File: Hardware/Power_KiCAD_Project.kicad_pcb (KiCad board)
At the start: 4 copper layers, 80 x 93.2 mm, 83 parts, among them J1 Barrel_Jack_MountingPin, J2 XT60 Cell 5, J3 XT60 Cell 4, J4 XT60 Cell 3, J5 XT60 Cell 2, J6 XT60 Cell 1, J7 XT60 To External Switch, J8 L717SDC37P1ACH4F, Q1 PSMN2R6-40YS, Q2 BSS84PH6327XTSA2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

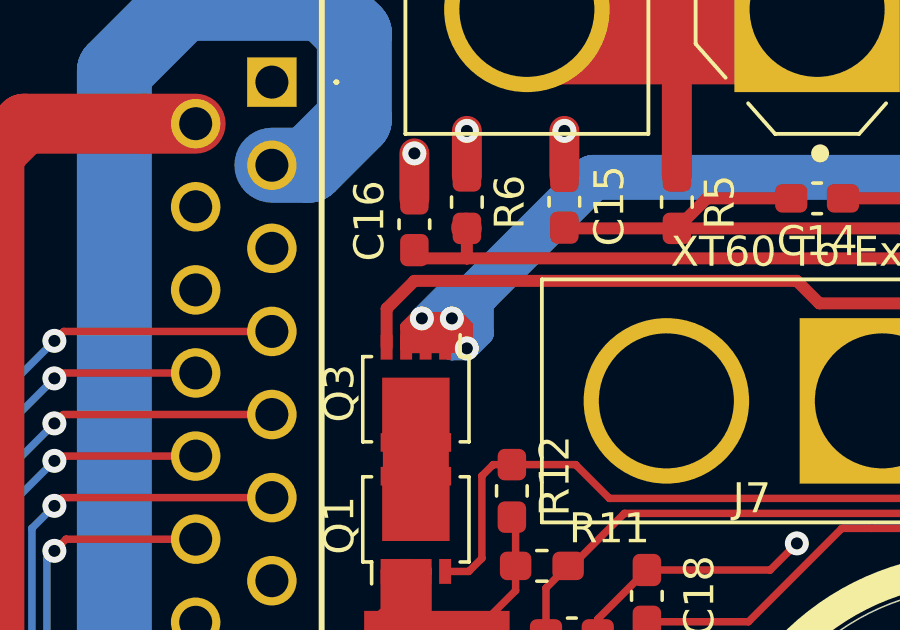
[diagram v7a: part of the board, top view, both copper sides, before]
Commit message: Adjustments to inner copper pours
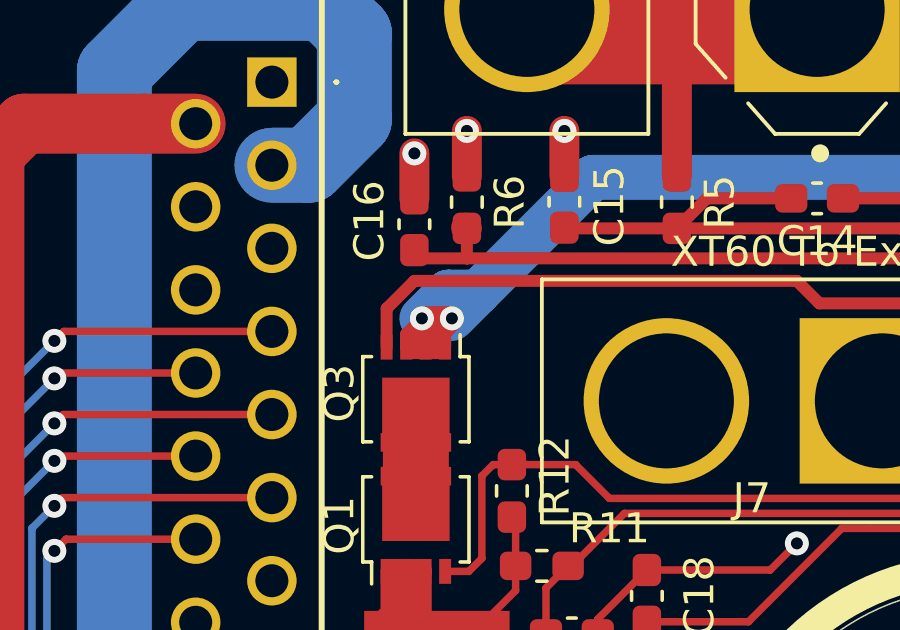
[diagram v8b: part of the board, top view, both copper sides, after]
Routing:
- net /LiPo Pack Monitor/PACK-: track 95.9 -> 82.5 mm, vias 4 -> 3
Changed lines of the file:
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@@
     (thickness 1.6)
     (drawings 27)
-    (tracks 936)
+    (tracks 909)
     (zones 0)
     (modules 83)
@@
     (user_trace_width 5)
     (trace_clearance 0.05)
-    (zone_clearance 1)
+    (zone_clearance 0.508)
     (zone_45_only no)
     (trace_min 0.09)
@@
   (segment (start 134 126.4) (end 135.25 126.4) (width 0.25) (layer B.Cu) (net 80))
   (segment (start 133.4 125.8) (end 134 126.4) (width 0.25) (layer B.Cu) (net 80))
-  (segment (start 98.774999 82.46) (end 98.124999 82.46) (width 0.4) (layer F.Cu) (net 147))
-  (segment (start 97.475 82.460001) (end 98.124999 82.46) (width 0.4) (layer F.Cu) (net 147))
-  (segment (start 98.775 82.46) (end 99.21 82.46) (width 0.4) (layer F.Cu) (net 147))
-  (segment (start 98.125 82.46) (end 98.29 82.46) (width 0.4) (layer F.Cu) (net 147))
-  (segment (start 97.475 82.46) (end 97.475 82.275) (width 0.4) (layer F.Cu) (net 147))
-  (segment (start 98.315 82) (end 98.775 82.46) (width 0.4) (layer F.Cu) (net 147))
-  (segment (start 97.475 82.275) (end 97.75 82) (width 0.4) (layer F.Cu) (net 147))
-  (segment (start 97.75 82) (end 98.315 82) (width 0.4) (layer F.Cu) (net 147))
-  (segment (start 97.75 82) (end 98.25 81.5) (width 0.4) (layer F.Cu) (net 147))
-  (segment (start 97.75 82.085) (end 98.125 82.46) (width 0.4) (layer F.Cu) (net 147))
-  (segment (start 97.75 82) (end 97.75 82.085) (width 0.4) (layer F.Cu) (net 147))
-  (segment (start 98.25 81.5) (end 99 81.5) (width 0.4) (layer F.Cu) (net 147))
-  (segment (start 98.25 81.5) (end 98.75 82) (width 0.4) (layer F.Cu) (net 147))
-  (segment (start 98.29 82.46) (end 98.75 82) (width 0.4) (layer F.Cu) (net 147))
-  (segment (start 98.75 81.5) (end 99 81.75) (width 0.4) (layer F.Cu) (net 147))
-  (segment (start 98.25 81.5) (end 98.75 81.5) (width 0.4) (layer F.Cu) (net 147))
-  (segment (start 99 81.75) (end 99.25 81.5) (width 0.4) (layer F.Cu) (net 147))
-  (segment (start 98.75 82) (end 99 81.75) (width 0.4) (layer F.Cu) (net 147))
-  (segment (start 99.5 81.75) (end 99.25 81.5) (width 0.4) (layer F.Cu) (net 147))
-  (segment (start 98.75 81.5) (end 99.5 82.25) (width 0.4) (layer F.Cu) (net 147))
-  (segment (start 98.25 81.5) (end 97.75 81.5) (width 0.4) (layer F.Cu) (net 147))
-  (segment (start 97.475 81.775) (end 97.475 82.46) (width 0.4) (layer F.Cu) (net 147))
-  (segment (start 97.75 81.5) (end 97.475 81.775) (width 0.4) (layer F.Cu) (net 147))
-  (segment (start 99.5 82.5) (end 99.5 81.75) (width 0.4) (layer F.Cu) (net 147))
-  (via (at 99.5 82.5) (size 0.8) (drill 0.4) (layers F.Cu B.Cu) (net 147))
   (via (at 120.5 83.25) (size 0.8) (drill 0.4) (layers F.Cu B.Cu) (net 147))
   (segment (start 120.375 83.125) (end 120.5 83.25) (width 0.4) (layer F.Cu) (net 147))
   (segment (start 119.25 83.125) (end 120.375 83.125) (width 0.4) (layer F.Cu) (net 147))
-  (segment (start 99 81.5) (end 99.25 81.5) (width 0.4) (layer F.Cu) (net 147))
   (via (at 99 81.5) (size 0.8) (drill 0.4) (layers F.Cu B.Cu) (net 147))
-  (segment (start 97.75 81.5) (end 97.75 81.5) (width 0.4) (layer F.Cu) (net 147))
   (via (at 98 81.5) (size 0.8) (drill 0.4) (layers F.Cu B.Cu) (net 147))
   (segment (start 154.5 71.25) (end 151 67.75) (width 1.5) (layer B.Cu) (net 147))
   (segment (start 154.5 75.25) (end 154.5 71.25) (width 1.5) (layer B.Cu) (net 147))
   (segment (start 152.950001 76.799999) (end 154.5 75.25) (width 1.5) (layer B.Cu) (net 147))
-  (segment (start 98.875 80.625) (end 99.875 80.625) (width 0.8) (layer B.Cu) (net 147))
-  (segment (start 98 81.5) (end 98.875 80.625) (width 0.8) (layer B.Cu) (net 147))
   (segment (start 99.875 80.625) (end 103.700001 76.799999) (width 1.5) (layer B.Cu) (net 147))
-  (segment (start 99 81.5) (end 99.875 80.625) (width 1.5) (layer B.Cu) (net 147))
-  (segment (start 99.5 82) (end 99 81.5) (width 0.8) (layer B.Cu) (net 147))
-  (segment (start 99.5 82.5) (end 99.5 82) (width 0.8) (layer B.Cu) (net 147))
-  (segment (start 99 82.5) (end 98 81.5) (width 0.8) (layer B.Cu) (net 147))
-  (segment (start 99.5 82.5) (end 99 82.5) (width 0.8) (layer B.Cu) (net 147))
-  (segment (start 99.5 82.5) (end 100 82) (width 0.8) (layer B.Cu) (net 147))
   (segment (start 100 80.75) (end 99.875 80.625) (width 0.8) (layer B.Cu) (net 147))
-  (segment (start 100 82) (end 100 80.75) (width 0.8) (layer B.Cu) (net 147))
   (segment (start 120.5 76.849998) (end 120.549999 76.799999) (width 0.4) (layer B.Cu) (net 147))
   (segment (start 120.5 83.25) (end 120.5 76.849998) (width 0.4) (layer B.Cu) (net 147))
   (segment (start 120.549999 76.799999) (end 152.950001 76.799999) (width 1.5) (layer B.Cu) (net 147))
   (segment (start 103.700001 76.799999) (end 120.549999 76.799999) (width 1.5) (layer B.Cu) (net 147))
-  (segment (start 99 82) (end 98.75 82) (width 0.4) (layer F.Cu) (net 147))
-  (segment (start 99.5 82.5) (end 99 82) (width 0.4) (layer F.Cu) (net 147))
+  (segment (start 99 81.5) (end 99.875 80.625) (width 1.5) (layer B.Cu) (net 147))
+  (segment (start 98.875 80.625) (end 99.875 80.625) (width 1.5) (layer B.Cu) (net 147))
+  (segment (start 98 81.5) (end 98.875 80.625) (width 1.5) (layer B.Cu) (net 147))
+  (segment (start 97.475 82.025) (end 98 81.5) (width 0.4) (layer F.Cu) (net 147))
+  (segment (start 97.475 82.46) (end 97.475 82.025) (width 0.4) (layer F.Cu) (net 147))
+  (segment (start 98.775 81.725) (end 99 81.5) (width 0.4) (layer F.Cu) (net 147))
+  (segment (start 98.775 82.46) (end 98.775 81.725) (width 0.4) (layer F.Cu) (net 147))
+  (segment (start 99 81.5) (end 98 81.5) (width 0.8) (layer F.Cu) (net 147))
+  (segment (start 97.675 82.46) (end 98.575 82.46) (width 0.8) (layer F.Cu) (net 147))
+  (segment (start 99 81.5) (end 98.575 81.925) (width 0.8) (layer F.Cu) (net 147))
+  (segment (start 98.575 81.925) (end 98 81.925) (width 0.8) (layer F.Cu) (net 147))
   (zone (net 3) (net_name +3V3) (layer 3.3V.Cu) (hatch edge 0.508)
     (connect_pads (clearance 0.508))
     (min_thickness 0.254)
-    (fill yes (arc_segments 32) (thermal_gap 0.508) (thermal_bridge_width 0.508) (smoothing fillet) (radius 2))
+    (fill yes (arc_segments 32) (thermal_gap 0.508) (thermal_bridge_width 0.508) (smoothing fillet) (radius 1.5))
     (polygon
       (pts
@@
       (pts
         (xy 109 95.75) (xy 108.5 99.25) (xy 96.25 99.25) (xy 96.25 85) (xy 103 85)
-        (xy 103 81.25) (xy 109 81.25)
+        (xy 103 84.25) (xy 109 84.25)
       )
     )
@@
     (connect_pads (clearance 1))
     (min_thickness 0.254)
-    (fill yes (arc_segments 32) (thermal_gap 0.508) (thermal_bridge_width 0.508))
+    (fill yes (arc_segments 32) (thermal_gap 0.508) (thermal_bridge_width 0.508) (smoothing fillet) (radius 1.5))
     (polygon
       (pts
         (xy 157 86.5) (xy 147.5 86.5) (xy 147.5 88.5) (xy 125.25 88.5) (xy 125.25 90)
-        (xy 115.75 90) (xy 110.25 93.375) (xy 110.25 80.125) (xy 101.25 80) (xy 101.25 83)
-        (xy 96.25 83) (xy 96.25 59.25) (xy 157 59.25)
+        (xy 115.75 90) (xy 110.25 93.375) (xy 110.25 87.95) (xy 110.7 87.95) (xy 110.7 80.25)
+        (xy 101.25 80.25) (xy 101.25 83.25) (xy 96.25 83.25) (xy 96.25 59.25) (xy 157 59.25)
       )
     )
@@
         (xy 157.25 116.75) (xy 151.5 116.75) (xy 151.5 113.25) (xy 155.75 113.25) (xy 155.75 112.75)
         (xy 151 112.75) (xy 151 117.25) (xy 157.25 117.25) (xy 157.25 137.5) (xy 82 137.5)
-        (xy 82 59.5) (xy 95 59.5) (xy 95 101) (xy 108.75 101) (xy 110.25 103.5)
-        (xy 111.5 104.75) (xy 113.25 105.75) (xy 116 106.5) (xy 119.25 106) (xy 121.75 104.5)
-        (xy 123.25 102.75) (xy 124 101.25) (xy 124.5 98.75) (xy 124.25 96.5) (xy 122.75 93.5)
-        (xy 120.75 91.75) (xy 127 91.75) (xy 127 89.75) (xy 148.75 89.75) (xy 148.75 87.75)
-        (xy 157.25 87.75)
+        (xy 82 59.5) (xy 95 59.5) (xy 95 73.85) (xy 94 73.85) (xy 94 76.25)
+        (xy 95 76.25) (xy 95 96.75) (xy 94 96.75) (xy 94 101.25) (xy 109 101.25)
+        (xy 110.25 103.5) (xy 111.5 104.75) (xy 113.25 105.75) (xy 116 106.5) (xy 119.25 106)
+        (xy 121.75 104.5) (xy 123.25 102.75) (xy 124 101.25) (xy 124.5 98.75) (xy 124.25 96.5)
+        (xy 122.75 93.5) (xy 120.75 91.75) (xy 127 91.75) (xy 127 89.75) (xy 148.75 89.75)
+        (xy 148.75 87.75) (xy 157.25 87.75)
       )
     )
